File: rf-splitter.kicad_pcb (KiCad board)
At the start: 2 copper layers, 0 parts

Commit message: Adding the PCB layout
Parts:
- added G***: LOGO, lib:spacelab-logo, F.Cu at (125.7, 70.3)
- added H1: MountingHole, MountingHole:MountingHole_3.2mm_M3_ISO14580_Pad_TopBottom, F.Cu at (88.9, 50.8)
- added H2: MountingHole, MountingHole:MountingHole_3.2mm_M3_ISO14580_Pad_TopBottom, F.Cu at (162.6, 50.8)
- added H3: MountingHole, MountingHole:MountingHole_3.2mm_M3_ISO14580_Pad_TopBottom, F.Cu at (85.1, 136.6)
- added H4: MountingHole, MountingHole:MountingHole_3.2mm_M3_ISO14580_Pad_TopBottom, F.Cu at (165.1, 136.6)
- added J1: ESQ-126-34-G-D, lib:SAMTEC_ESQ-126-34-G-D, F.Cu at (94.0, 50.8)
- added J2: ESQ-126-34-G-D, lib:SAMTEC_ESQ-126-34-G-D, F.Cu at (94.0, 55.9)
- added REF**: OSHW-Logo2_9.8x8mm_SilkScreen, Symbol:OSHW-Logo2_9.8x8mm_SilkScreen, F.Cu at (144.0, 117.8)
- added U1: Z99SC-62-S+, Z99SC-62-S:Z99SC-62-S+, F.Cu at (125.7, 97.5)
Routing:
- added copper zone on B.Cu, net (none)
- added copper zone on F.Cu, net (none)
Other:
- board outline added: 86.6 x 92.2 mm
- board text added: "RF-Splitter v1.0"

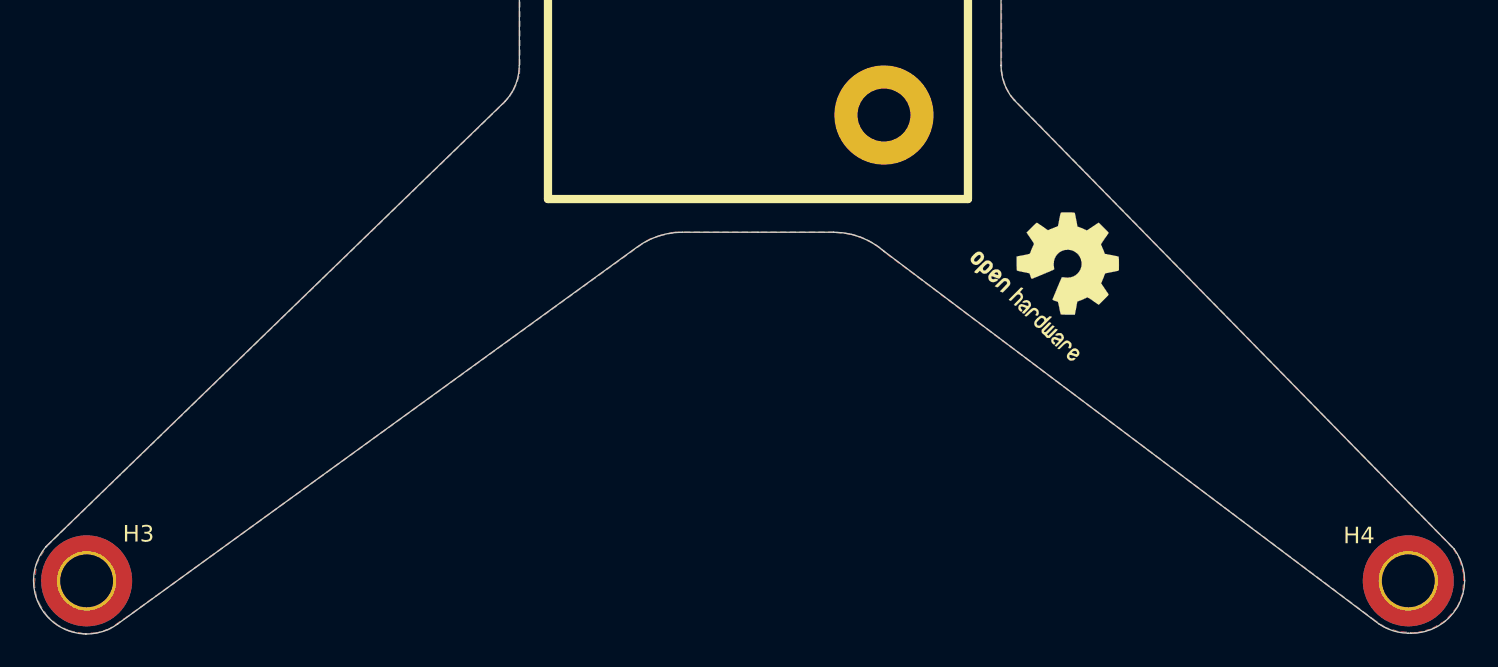
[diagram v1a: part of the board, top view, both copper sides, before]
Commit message: Fixing the position of the mounting holes. closes #5
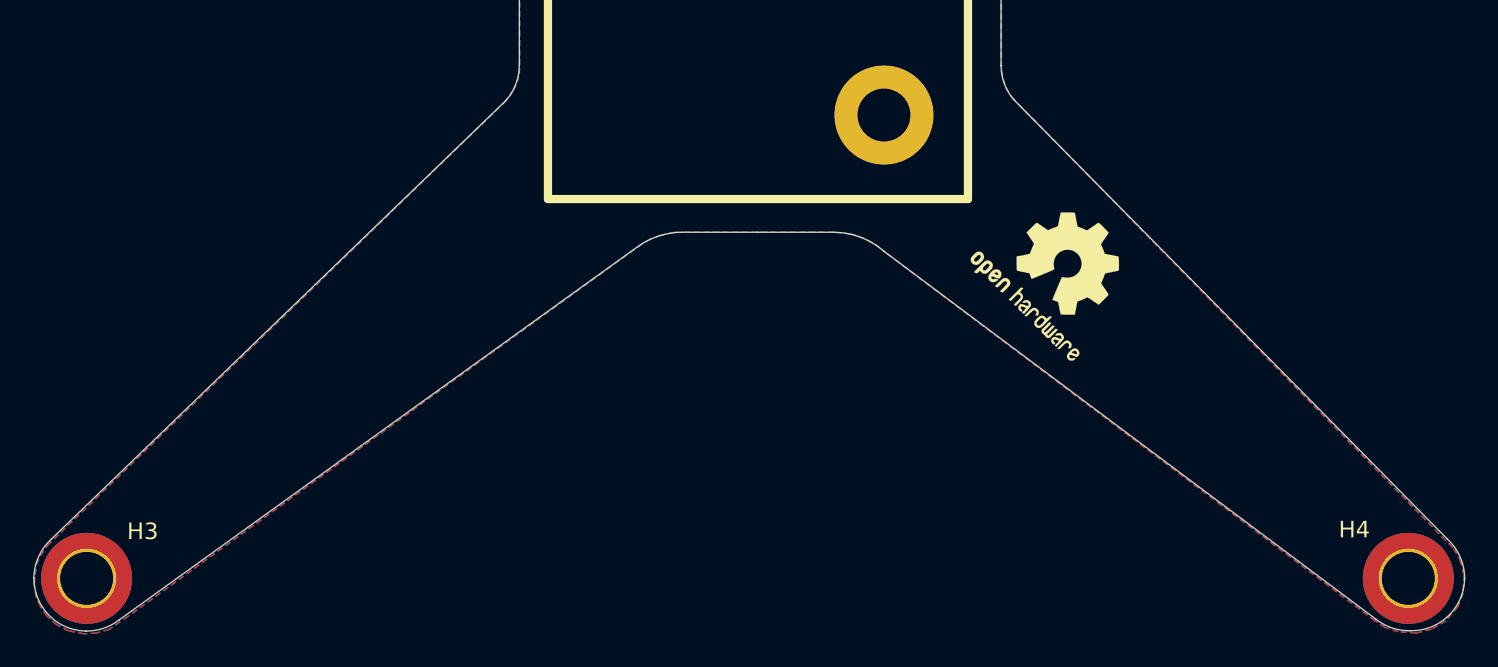
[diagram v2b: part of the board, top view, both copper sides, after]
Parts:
- moved H3 0.15 mm to (85.1, 136.4)
- moved H4 0.15 mm to (165.1, 136.4)
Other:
- board size 86.6 x 92.2 mm -> 86.5 x 92 mm
